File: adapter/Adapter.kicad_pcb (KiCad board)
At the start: 4 copper layers, 45.5 x 50 mm, 58 parts, among them J1 USB_B_Micro, J2 2040210-1, J3 USB_C_Receptacle, J4 Conn_01x05_Male, J5 Conn_01x03_Male, Q1 IRLML2244TRPBF, SW1 RESET, SW2 BOOT, U1 SN75DP119RGYT, U2 LD1117S33TR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

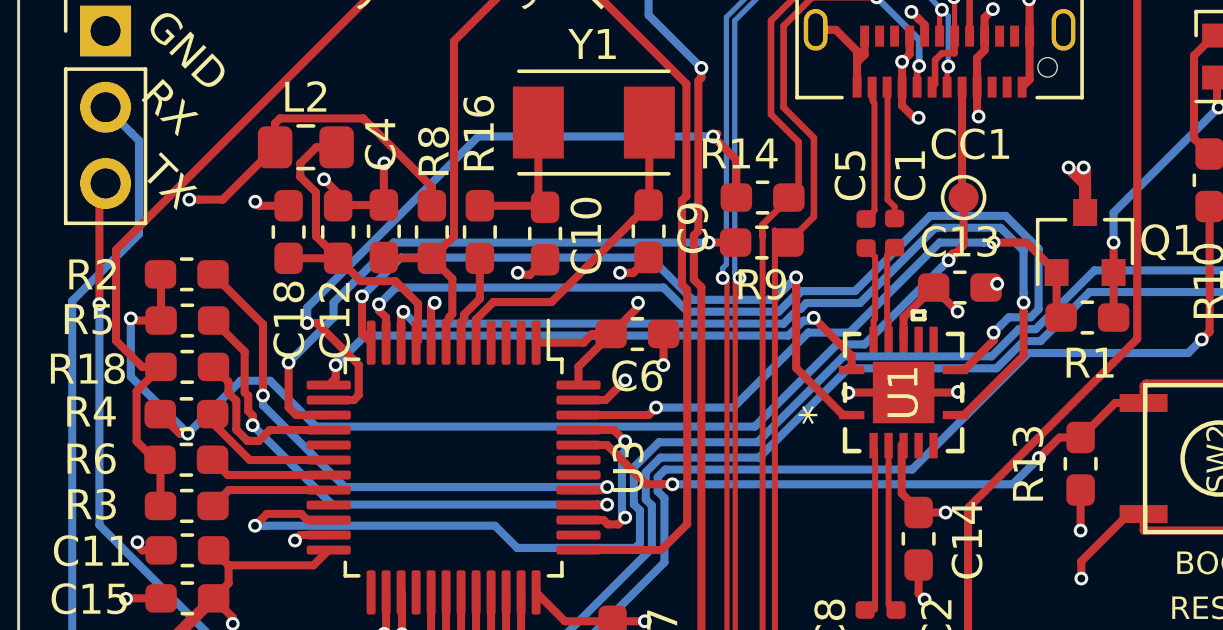
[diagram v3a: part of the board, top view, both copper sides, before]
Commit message: fix the PA1 connection (the cheap way, as in prototype)
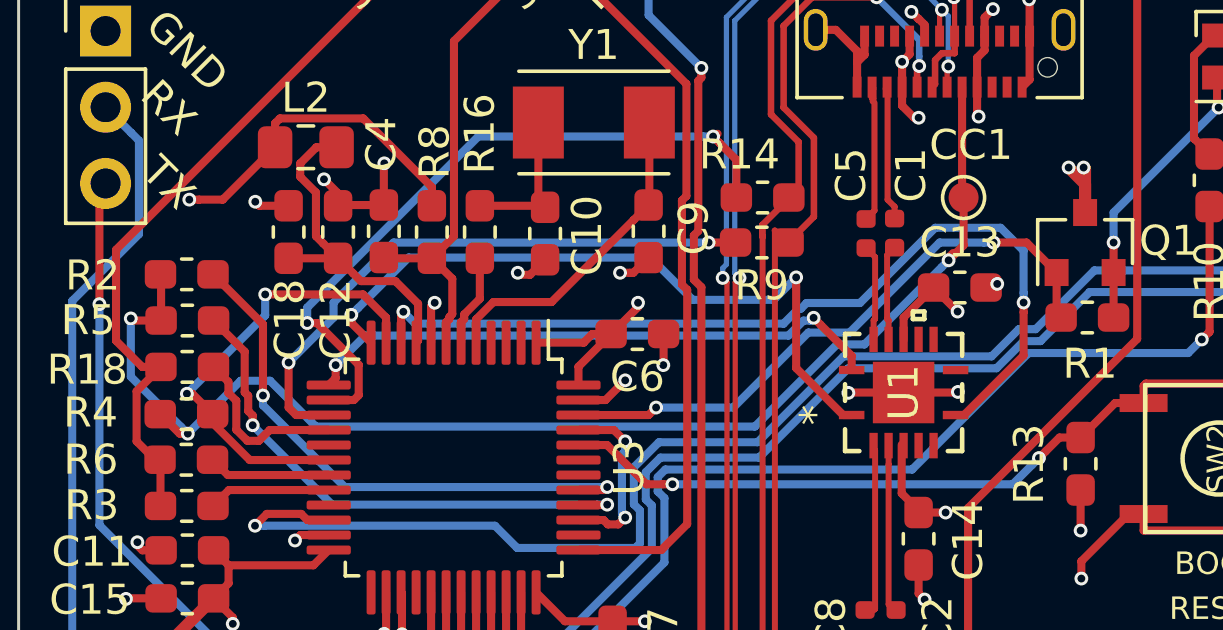
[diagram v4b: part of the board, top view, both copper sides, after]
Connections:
- U3 pad 11: EQ_CTL -> /CC1_RX
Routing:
- net EQ_CTL: track 31.5 -> 0.00 mm, vias 2 -> 0
- net /CC1_RX: track 4.67 -> 15.4 mm, vias 0 -> 2
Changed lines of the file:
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@@
     (thickness 1.6)
     (drawings 16)
-    (tracks 801)
+    (tracks 785)
     (zones 0)
     (modules 58)
@@
       (net 14 PRE_CTL))
     (pad 11 smd roundrect (at -4.1625 2.25 270) (size 1.475 0.3) (layers F.Cu F.Paste F.Mask) (roundrect_rratio 0.25)
-      (net 20 EQ_CTL))
+      (net 51 /CC1_RX))
     (pad 10 smd roundrect (at -4.1625 1.75 270) (size 1.475 0.3) (layers F.Cu F.Paste F.Mask) (roundrect_rratio 0.25)
       (net 19 EN_CTL))
@@
   (segment (start 51.905032 51.602989) (end 52.000031 51.50799) (width 0.27) (layer B.Cu) (net 13))
   (segment (start 37.052969 52.101031) (end 51.163259 52.10103) (width 0.27) (layer B.Cu) (net 13))
-  (via (at 36.947778 50.794245) (size 0.46) (drill 0.26) (layers F.Cu B.Cu) (net 14))
-  (segment (start 37.25 52.3375) (end 36.947778 52.035278) (width 0.27) (layer F.Cu) (net 14))
-  (segment (start 36.947778 51.119514) (end 36.947778 50.794245) (width 0.27) (layer F.Cu) (net 14))
-  (segment (start 36.947778 52.035278) (end 36.947778 51.119514) (width 0.27) (layer F.Cu) (net 14))
   (segment (start 51.418461 50.486723) (end 51.418461 50.161454) (width 0.27) (layer F.Cu) (net 14))
   (via (at 51.418461 50.161454) (size 0.46) (drill 0.26) (layers F.Cu B.Cu) (net 14))
@@
   (segment (start 53.269 54.750001) (end 52.984012 54.750001) (width 0.27) (layer F.Cu) (net 14))
   (segment (start 52.984012 54.750001) (end 51.418461 53.18445) (width 0.27) (layer F.Cu) (net 14))
-  (segment (start 51.188462 50.391453) (end 51.418461 50.161454) (width 0.27) (layer B.Cu) (net 14))
-  (segment (start 50.669915 50.91) (end 51.188462 50.391453) (width 0.27) (layer B.Cu) (net 14))
-  (segment (start 47.97 50.91) (end 50.669915 50.91) (width 0.27) (layer B.Cu) (net 14))
-  (segment (start 46.56 49.5) (end 47.97 50.91) (width 0.27) (layer B.Cu) (net 14))
-  (segment (start 38.242023 49.5) (end 46.56 49.5) (width 0.27) (layer B.Cu) (net 14))
-  (segment (start 36.947778 50.794245) (end 38.242023 49.5) (width 0.27) (layer B.Cu) (net 14))
+  (via (at 36.59 51.41) (size 0.46) (drill 0.26) (layers F.Cu B.Cu) (net 14))
+  (segment (start 36.59 51.6775) (end 36.59 51.41) (width 0.27) (layer F.Cu) (net 14))
+  (segment (start 38.5 49.5) (end 36.819999 51.180001) (width 0.27) (layer B.Cu) (net 14))
+  (segment (start 36.819999 51.180001) (end 36.59 51.41) (width 0.27) (layer B.Cu) (net 14))
+  (segment (start 46.56 49.5) (end 38.5 49.5) (width 0.27) (layer B.Cu) (net 14))
+  (segment (start 50.669915 50.91) (end 47.97 50.91) (width 0.27) (layer B.Cu) (net 14))
+  (segment (start 47.97 50.91) (end 46.56 49.5) (width 0.27) (layer B.Cu) (net 14))
+  (segment (start 37.25 52.3375) (end 36.59 51.6775) (width 0.27) (layer F.Cu) (net 14))
+  (segment (start 51.418461 50.161454) (end 50.669915 50.91) (width 0.27) (layer B.Cu) (net 14))
   (segment (start 54.83916 68.257279) (end 54.83916 70.31978) (width 0.2032) (layer F.Cu) (net 15))
   (segment (start 55.13596 67.960479) (end 54.83916 68.257279) (width 0.2032) (layer F.Cu) (net 15))
@@
   (segment (start 59 50.674731) (end 59 51) (width 0.27) (layer B.Cu) (net 19))
   (segment (start 56.053459 48.507999) (end 58.236163 48.507999) (width 0.27) (layer B.Cu) (net 19))
-  (segment (start 37.75 52.3375) (end 37.75 51.5) (width 0.27) (layer F.Cu) (net 20))
-  (segment (start 37.75 51.5) (end 37.51303 51.26303) (width 0.27) (layer F.Cu) (net 20))
-  (segment (start 37.51303 51.26303) (end 37.51303 51.061082) (width 0.27) (layer F.Cu) (net 20))
-  (via (at 37.51303 51.061082) (size 0.46) (drill 0.26) (layers F.Cu B.Cu) (net 20))
-  (via (at 58 52) (size 0.46) (drill 0.26) (layers F.Cu B.Cu) (net 20))
-  (segment (start 57.015988 53.249999) (end 58 52.265987) (width 0.27) (layer F.Cu) (net 20))
-  (segment (start 58 52.265987) (end 58 52) (width 0.27) (layer F.Cu) (net 20))
-  (segment (start 56.731 53.249999) (end 57.015988 53.249999) (width 0.27) (layer F.Cu) (net 20))
-  (segment (start 51.599422 50.618977) (end 53.381023 50.618977) (width 0.27) (layer B.Cu) (net 20))
-  (segment (start 53.381023 50.618977) (end 55.889012 48.110988) (width 0.27) (layer B.Cu) (net 20))
-  (segment (start 55.889012 48.110988) (end 58.40061 48.110988) (width 0.27) (layer B.Cu) (net 20))
-  (segment (start 58.229999 51.770001) (end 58 52) (width 0.27) (layer B.Cu) (net 20))
-  (segment (start 59.5 51.228164) (end 59.236162 51.492002) (width 0.27) (layer B.Cu) (net 20))
-  (segment (start 59.5 49.210378) (end 59.5 51.228164) (width 0.27) (layer B.Cu) (net 20))
-  (segment (start 50.834363 51.30701) (end 51.332406 50.808967) (width 0.27) (layer B.Cu) (net 20))
-  (segment (start 37.51303 51.061082) (end 38.074112 50.5) (width 0.27) (layer B.Cu) (net 20))
-  (segment (start 47.805553 51.307011) (end 50.834363 51.30701) (width 0.27) (layer B.Cu) (net 20))
-  (segment (start 46.998542 50.5) (end 47.805553 51.307011) (width 0.27) (layer B.Cu) (net 20))
-  (segment (start 58.507998 51.492002) (end 58.229999 51.770001) (width 0.27) (layer B.Cu) (net 20))
-  (segment (start 51.332406 50.808967) (end 51.409432 50.808967) (width 0.27) (layer B.Cu) (net 20))
-  (segment (start 38.074112 50.5) (end 46.998542 50.5) (width 0.27) (layer B.Cu) (net 20))
-  (segment (start 59.236162 51.492002) (end 58.507998 51.492002) (width 0.27) (layer B.Cu) (net 20))
-  (segment (start 58.40061 48.110988) (end 59.5 49.210378) (width 0.27) (layer B.Cu) (net 20))
-  (segment (start 51.409432 50.808967) (end 51.599422 50.618977) (width 0.27) (layer B.Cu) (net 20))
   (segment (start 54.4 43.87) (end 54.45 43.82) (width 0.2) (layer F.Cu) (net 21))
   (segment (start 54.466409 47.571409) (end 54.466409 43.836409) (width 0.2032) (layer F.Cu) (net 21))
@@
   (segment (start 33.206416 56.25) (end 31.97 55.013584) (width 0.27) (layer F.Cu) (net 51))
   (segment (start 35.8375 56.25) (end 33.206416 56.25) (width 0.27) (layer F.Cu) (net 51))
+  (via (at 33.72 50.73) (size 0.46) (drill 0.26) (layers F.Cu B.Cu) (net 51))
+  (segment (start 36.98 50.73) (end 33.72 50.73) (width 0.27) (layer F.Cu) (net 51))
+  (segment (start 37.75 52.3375) (end 37.75 51.5) (width 0.27) (layer F.Cu) (net 51))
+  (segment (start 37.75 51.5) (end 36.98 50.73) (width 0.27) (layer F.Cu) (net 51))
+  (via (at 31.11 54.04) (size 0.46) (drill 0.26) (layers F.Cu B.Cu) (net 51))
+  (segment (start 33.72 50.73) (end 33.72 51.43) (width 0.27) (layer B.Cu) (net 51))
+  (segment (start 33.72 51.43) (end 31.11 54.04) (width 0.27) (layer B.Cu) (net 51))
+  (segment (start 31.29 54.04) (end 31.97 54.72) (width 0.27) (layer F.Cu) (net 51))
+  (segment (start 31.11 54.04) (end 31.29 54.04) (width 0.27) (layer F.Cu) (net 51))
   (segment (start 54.9365 57.3615) (end 55.35 57.775) (width 0.27) (layer F.Cu) (net 52))
   (segment (start 54.9365 55.7375) (end 54.9365 57.3615) (width 0.27) (layer F.Cu) (net 52))

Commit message: enter unpopulated parts note
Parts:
- MH1, MH2, MH3, MH4: value MountingHole -> MOUNTHOLE
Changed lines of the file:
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@@
   (module SN75DP119:SN75DP119RGYT (layer F.Cu)
     (at 55 54 90)
+    (attr smd)
     (fp_text reference U1 (at 0 0 90) (layer F.SilkS)
       (effects (font (size 1 1) (thickness 0.15)))
@@
       (effects (font (size 1 1) (thickness 0.15)))
     )
-    (fp_text value MountingHole (at 0 3.5) (layer F.Fab)
+    (fp_text value MOUNTHOLE (at 0 3.5) (layer F.Fab)
       (effects (font (size 1 1) (thickness 0.15)))
     )
@@
       (effects (font (size 1 1) (thickness 0.15)))
     )
-    (fp_text value MountingHole (at 0 3.5) (layer F.Fab)
+    (fp_text value MOUNTHOLE (at 0 3.5) (layer F.Fab)
       (effects (font (size 1 1) (thickness 0.15)))
     )
@@
       (effects (font (size 1 1) (thickness 0.15)))
     )
-    (fp_text value MountingHole (at 0 3.5) (layer F.Fab)
+    (fp_text value MOUNTHOLE (at 0 3.5) (layer F.Fab)
       (effects (font (size 1 1) (thickness 0.15)))
     )
@@
       (effects (font (size 1 1) (thickness 0.15)))
     )
-    (fp_text value MountingHole (at 0 3.5) (layer F.Fab)
-      (effects (font (size 1 1) (thickness 0.15)))
-    )
+    (fp_text value MOUNTHOLE (at 0 3.5) (layer F.Fab)
+      (effects (font (size 1 1) (thickness 0.15)))
+    )
